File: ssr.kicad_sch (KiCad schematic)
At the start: 2 parts, among them Q29 DMN60H080DS, Q30 DMN60H080DS

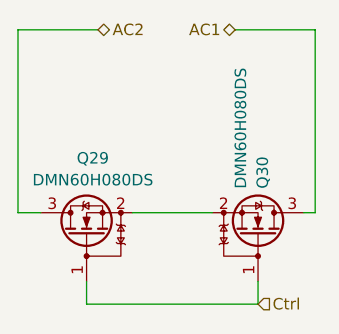
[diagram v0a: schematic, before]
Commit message: replace bcd logic with bin-to-dec module
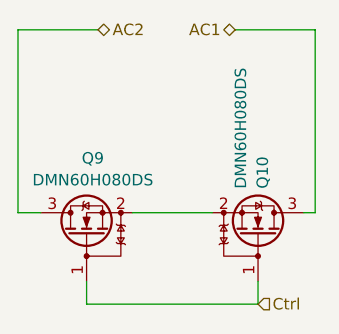
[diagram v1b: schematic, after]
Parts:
- renumbered Q30 to Q10, Q29 to Q9

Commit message: switched to using SSR module
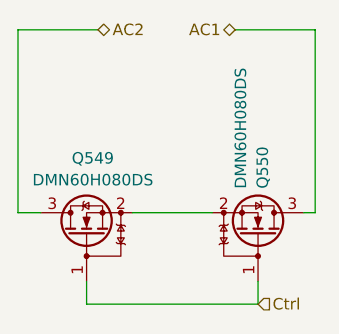
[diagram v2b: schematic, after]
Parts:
- renumbered Q9 to Q549, Q10 to Q550
